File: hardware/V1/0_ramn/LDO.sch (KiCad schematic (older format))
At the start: 4 parts, among them U3 NCV8163

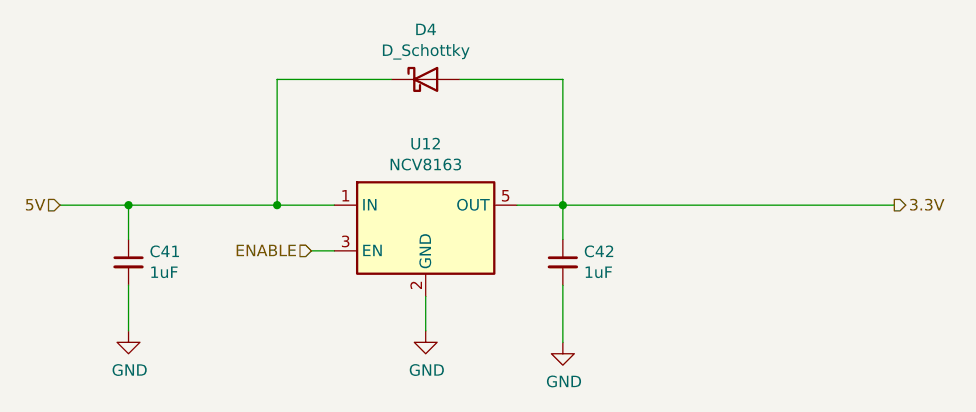
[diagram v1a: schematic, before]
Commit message: Updated schematics to show BOOT0 resistor settings for STM32L5 microcontrollers
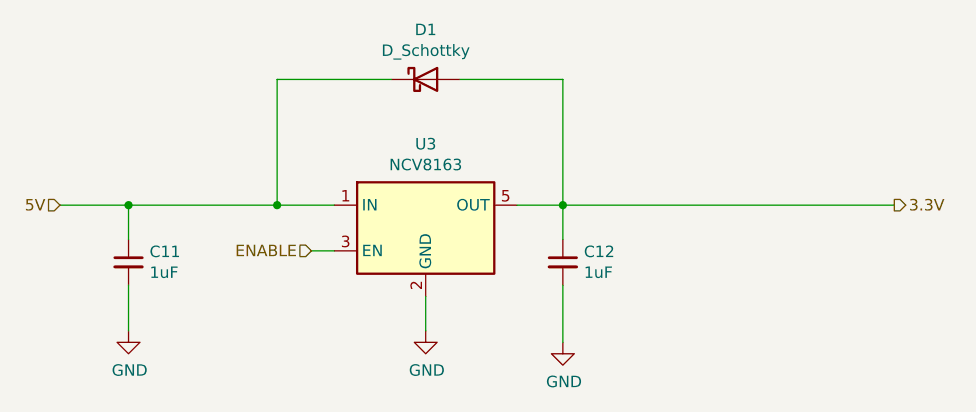
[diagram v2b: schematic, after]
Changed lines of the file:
@@
 $Descr A4 11693 8268
 encoding utf-8
-Sheet 9 9
+Sheet 3 9
 Title "RAMN: Resistant Automotive Miniature Network V1.0"
-Date "2021-06-01"
+Date "2024-02-20"
 Rev "B2L"
-Comp "Copyright (c) 2021 TOYOTA MOTOR CORPORATION. ALL RIGHTS RESERVED."
+Comp "Copyright (c) 2024 TOYOTA MOTOR CORPORATION. ALL RIGHTS RESERVED."
 Comment1 ""
 Comment2 ""
@@
 AR Path="/5D8EDE42/5D82B40A/5D80EE58" Ref="U9"  Part="1"
 AR Path="/5D7DEA89/5D7F286F/5D80EE58" Ref="U12"  Part="1"
-F 0 "U12" H 4500 3267 50  0000 C CNN
+F 0 "U3" H 4500 3267 50  0000 C CNN
 F 1 "NCV8163" H 4500 3176 50  0000 C CNN
 F 2 "Package_SO:TSOP-5_1.65x3.05mm_P0.95mm" H 4500 2500 50  0001 C CIN
@@
 AR Path="/5D8EDE42/5D82B40A/5D80EE60" Ref="C31"  Part="1"
 AR Path="/5D7DEA89/5D7F286F/5D80EE60" Ref="C41"  Part="1"
-F 0 "C41" H 3292 3096 50  0000 L CNN
+F 0 "C11" H 3292 3096 50  0000 L CNN
 F 1 "1uF" H 3292 3005 50  0000 L CNN
 F 2 "Capacitor_SMD:C_1206_3216Metric" H 3200 3050 50  0001 C CNN
@@
 AR Path="/5D8EDE42/5D82B40A/5D80EE66" Ref="C32"  Part="1"
 AR Path="/5D7DEA89/5D7F286F/5D80EE66" Ref="C42"  Part="1"
-F 0 "C42" H 5192 3096 50  0000 L CNN
+F 0 "C12" H 5192 3096 50  0000 L CNN
 F 1 "1uF" H 5192 3005 50  0000 L CNN
 F 2 "Capacitor_SMD:C_1206_3216Metric" H 5100 3050 50  0001 C CNN
@@
 AR Path="/5D8EDE42/5D82B40A/5D80EE76" Ref="#PWR060"  Part="1"
 AR Path="/5D7DEA89/5D7F286F/5D80EE76" Ref="#PWR079"  Part="1"
-F 0 "#PWR079" H 4500 3100 50  0001 C CNN
+F 0 "#PWR022" H 4500 3100 50  0001 C CNN
 F 1 "GND" H 4505 3177 50  0000 C CNN
 F 2 "" H 4500 3350 50  0001 C CNN
@@
 AR Path="/5D8EDE42/5D82B40A/5D80EE7C" Ref="#PWR061"  Part="1"
 AR Path="/5D7DEA89/5D7F286F/5D80EE7C" Ref="#PWR080"  Part="1"
-F 0 "#PWR080" H 5100 3150 50  0001 C CNN
+F 0 "#PWR023" H 5100 3150 50  0001 C CNN
 F 1 "GND" H 5105 3227 50  0000 C CNN
 F 2 "" H 5100 3400 50  0001 C CNN
@@
 AR Path="/5D8EDE42/5D82B40A/5D80EE8C" Ref="#PWR059"  Part="1"
 AR Path="/5D7DEA89/5D7F286F/5D80EE8C" Ref="#PWR078"  Part="1"
-F 0 "#PWR078" H 3200 3100 50  0001 C CNN
+F 0 "#PWR021" H 3200 3100 50  0001 C CNN
 F 1 "GND" H 3205 3177 50  0000 C CNN
 F 2 "" H 3200 3350 50  0001 C CNN
@@
 AR Path="/5D8EDE42/5D82B40A/60235D0A" Ref="D3"  Part="1"
 AR Path="/5D7DEA89/5D7F286F/60235D0A" Ref="D4"  Part="1"
-F 0 "D4" H 4500 2467 50  0000 C CNN
+F 0 "D1" H 4500 2467 50  0000 C CNN
 F 1 "D_Schottky" H 4500 2376 50  0000 C CNN
 F 2 "Diode_SMD:D_SOD-523" H 4500 2250 50  0001 C CNN
